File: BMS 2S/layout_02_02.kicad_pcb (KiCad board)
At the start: 2 copper layers, 64 x 36 mm, 26 parts

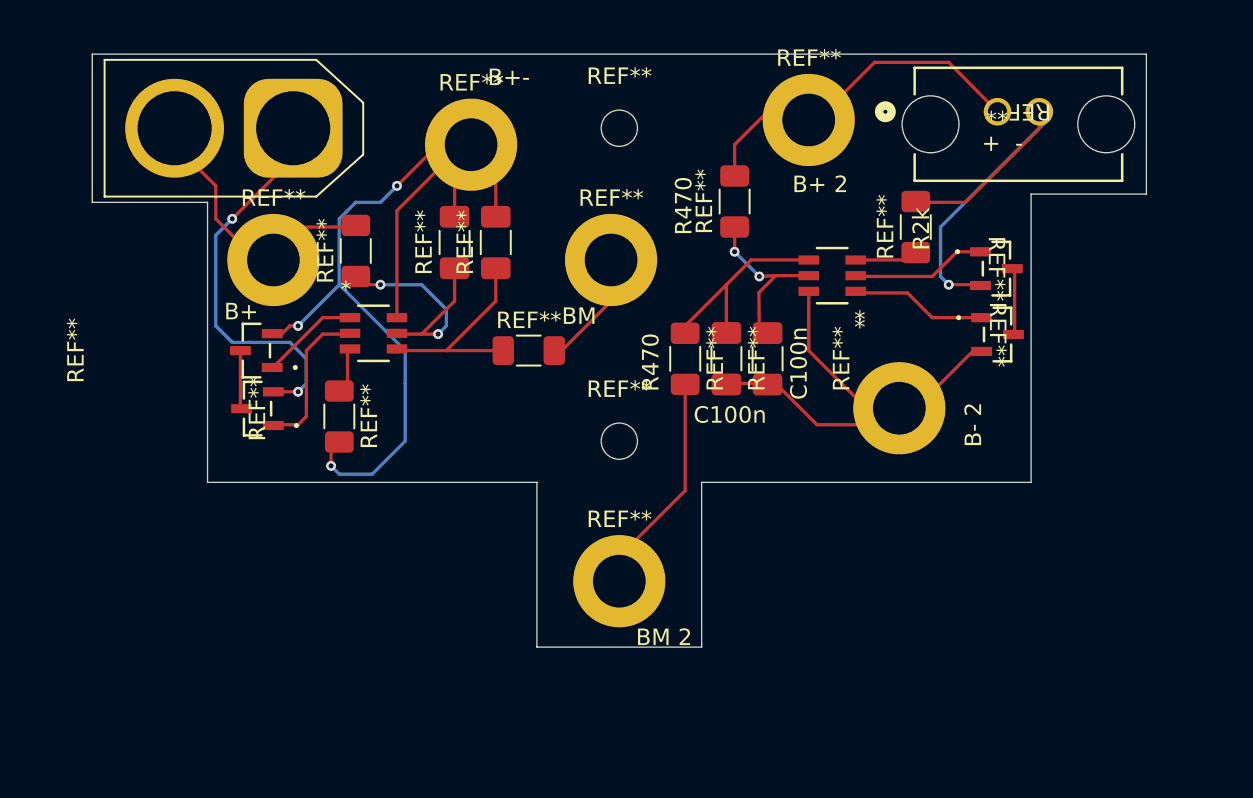
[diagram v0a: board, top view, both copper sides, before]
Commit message: BMS 2S, ajustement du design
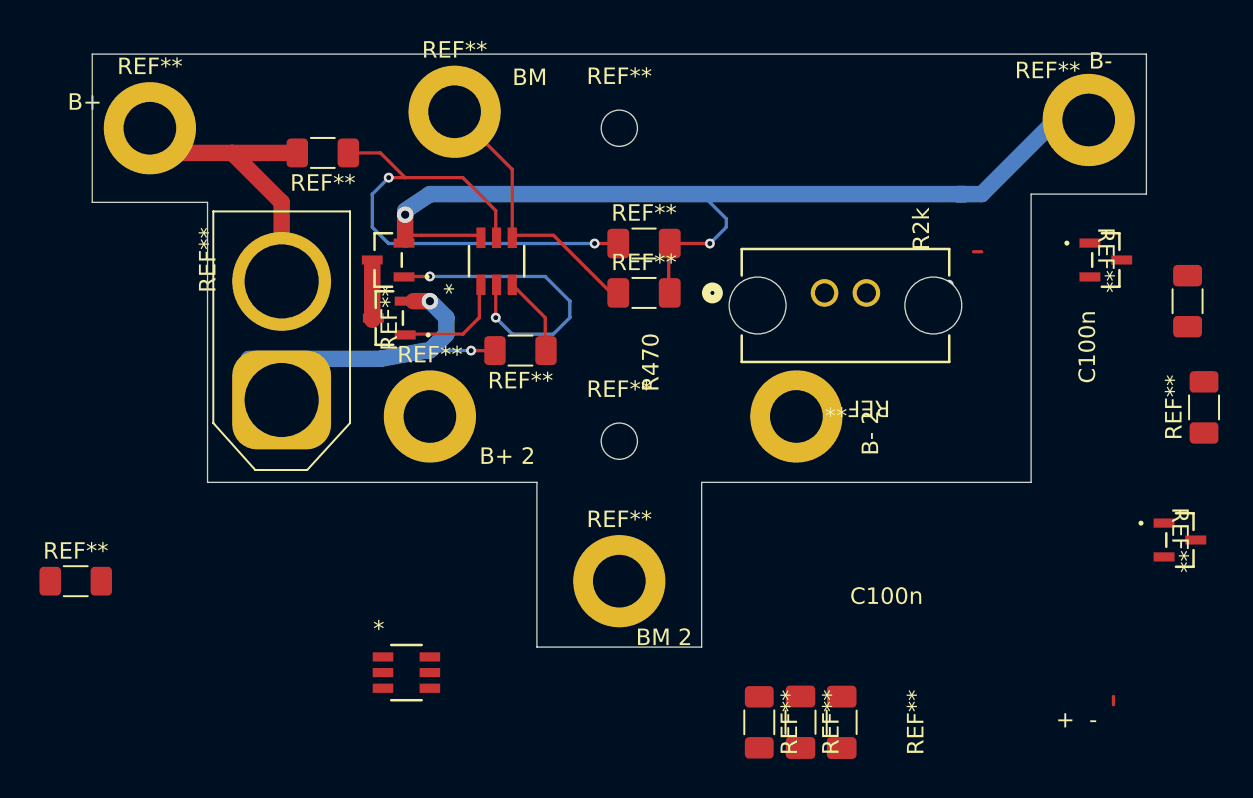
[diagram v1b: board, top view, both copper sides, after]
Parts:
- moved REF** 37.5 mm to (169.5, 75.0)
- moved REF** 31.1 mm to (176.5, 92.5)
- moved REF** 30.9 mm to (108.0, 103.0)
- moved REF** 29.2 mm to (129.5, 93.0)
- moved REF** 22.5 mm to (154.5, 111.6)
- moved REF** 22.5 mm to (152.0, 111.6)
- moved REF** 22.5 mm to (149.5, 111.6)
- moved REF** 20.7 mm to (128.1, 108.5)
- moved REF** 20.4 mm to (133.5, 83.6), turned to 90 degrees
- moved REF** 19.9 mm to (175.0, 100.5)
- moved REF** 17.1 mm to (175.5, 86.0)
- moved B+/- 16.5 mm to (120.5, 92.0), turned to 90 degrees
- moved REF** 15.2 mm to (153.5, 85.5)
- moved REF** 13.1 mm to (131.0, 74.5)
- moved REF** 11.9 mm to (142.5, 85.5), turned to 0 degrees
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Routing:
- net (no net): vias 10 -> 9
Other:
- board text added: "B-"
- board text removed: "B+-"
